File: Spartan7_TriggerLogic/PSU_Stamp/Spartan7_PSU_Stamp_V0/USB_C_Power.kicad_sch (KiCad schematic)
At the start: 4 parts, among them J1 USB4125-GF-A, U5 TPS7A2033

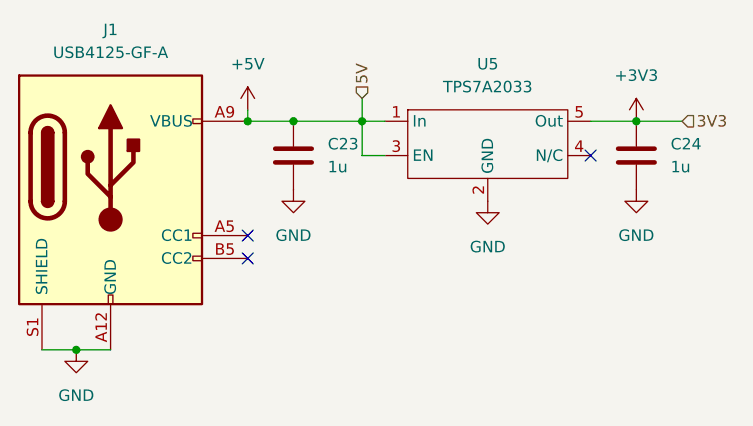
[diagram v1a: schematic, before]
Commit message: Add status LEDs and update power nets
Added new 0402 LEDs (D1, D4) and supporting resistor (R12) for power-good status indication. Updated net assignments and replaced a capacitor footprint with an LED. Modified schematic and PCB files to reflect these changes.
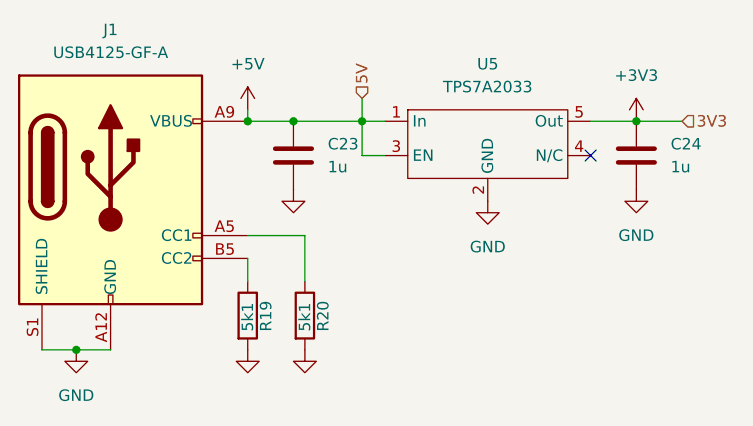
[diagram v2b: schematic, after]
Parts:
- added R19, R20: 5k1, Resistor_SMD:R_0402_1005Metric, symbol Device:R
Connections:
- net GND: now also R19.2, R20.2
- net at J1.A5 (CC1): now also R20.1
- net at J1.B5 (CC2): now also R19.1
- no-connect marks 3 -> 1
